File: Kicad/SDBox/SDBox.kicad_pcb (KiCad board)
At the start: 2 copper layers, 36.8 x 31.8 mm, 25 parts, among them J1 Amiga Parallel port, J2 PROG, J3 SD_Card, J4 USB_B_Micro, J5 USB_B_Mini, J6 POWER, U1 ATmega328-AU, U2 SPX3819M5-L-3-3, Y1 16M

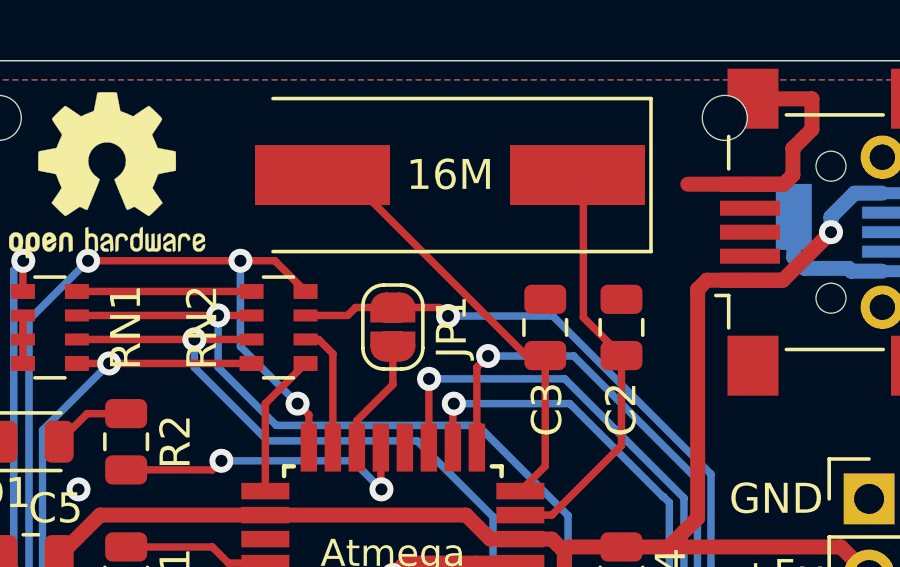
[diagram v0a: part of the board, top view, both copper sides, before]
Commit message: Added CSTCE crystal footprint
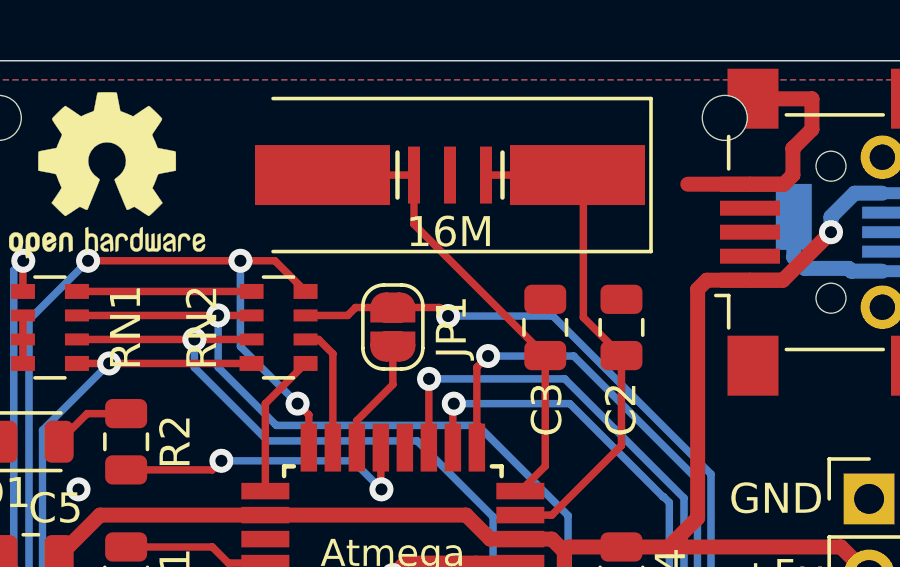
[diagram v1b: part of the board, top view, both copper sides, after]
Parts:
- added Y2: 16M, Sassa:MURATA_CSTCE, F.Cu at (126.4, 75.6)
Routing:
- net Net-(C2-Pad2): track 14.0 -> 17.0 mm
- net Net-(C3-Pad2): track 14.8 -> 15.7 mm

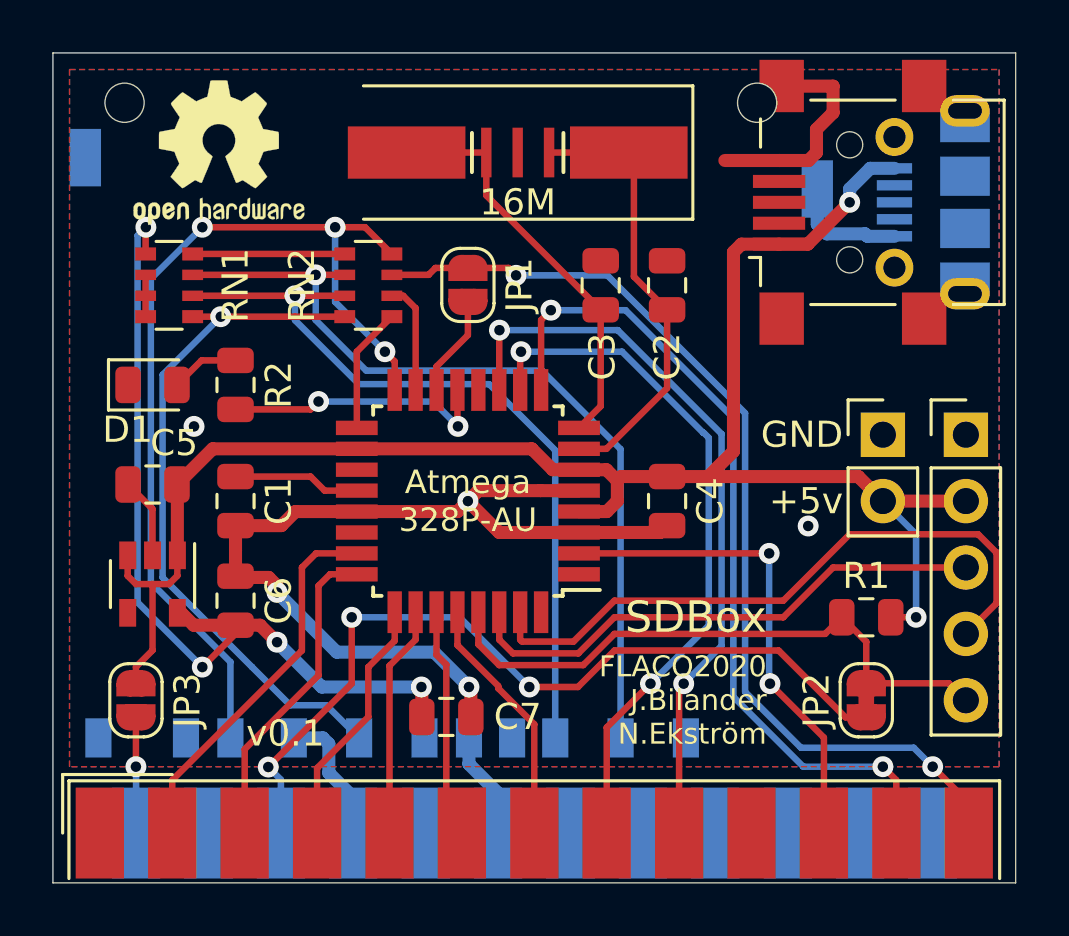
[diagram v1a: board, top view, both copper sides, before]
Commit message: Kicad : 0.2 with broken SPI programming port
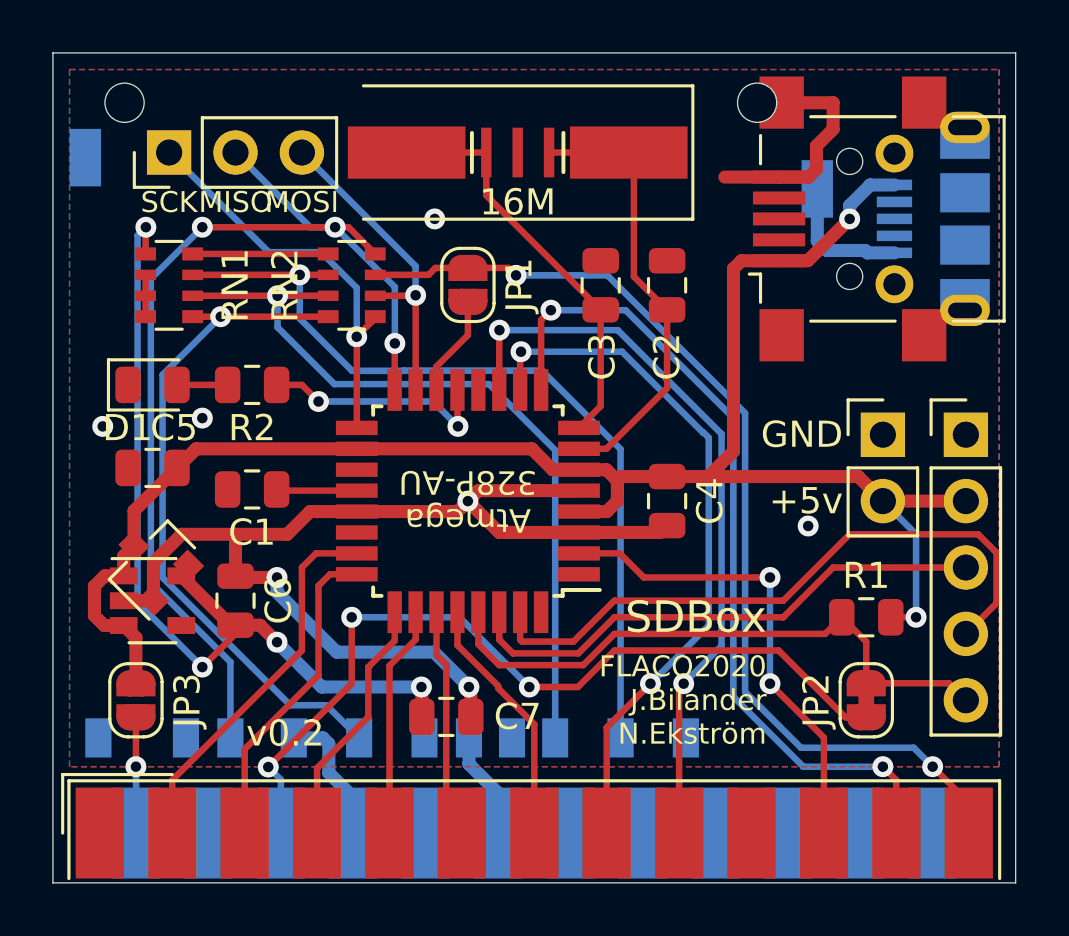
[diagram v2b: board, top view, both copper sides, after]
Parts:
- removed the J3 at (123.8, 73.7)
- added J2: SD_Card, Sassa:Conn_SDcard, B.Cu at (123.8, 73.7)
- added J7: PROG, Connector_PinHeader_2.54mm:PinHeader_1x03_P2.54mm_Vertical, F.Cu at (113.0, 75.6)
- added U20: XC6206PxxxMR, Package_TO_SOT_SMD:SOT-23, F.Cu at (112.4, 91.3)
- FID1: moved to B.Cu
- moved FID1 16.9 mm to (124.5, 89.5), turned to 180 degrees
- moved C1 0.78 mm to (116.2, 88.5), turned to 180 degrees
- moved C5 0.64 mm to (112.4, 87.6)
- moved J3 0.64 mm to (139.1, 78.1)
- moved J4 0.64 mm to (142.2, 78.1)
- moved R2 0.64 mm to (116.2, 84.5), turned to 180 degrees
- moved RN2 0.64 mm to (120.0, 80.6)
- moved U2 0.63 mm to (112.4, 92.7), turned to 0 degrees
- renumbered J5 to J3, J6 to J5, J2 to J6
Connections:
- J1 pad 1: (no net) -> Net-(J1-Pad1)
- J1 pad 10: (no net) -> Net-(J1-Pad10)
- J1 pad 15: (no net) -> Net-(J1-Pad15)
- J1 pad 23: (no net) -> Net-(J1-Pad23)
- J1 pad 24: (no net) -> Net-(J1-Pad24)
- J1 pad 25: (no net) -> Net-(J1-Pad25)
- J3 pad 2: (no net) -> Net-(J3-Pad2)
- J3 pad 3: (no net) -> Net-(J3-Pad3)
- J3 pad 4: (no net) -> Net-(J3-Pad4)
- J4 pad 2: (no net) -> Net-(J4-Pad2)
- J4 pad 3: (no net) -> Net-(J4-Pad3)
- J4 pad 4: (no net) -> Net-(J4-Pad4)
- U1 pad 1: (no net) -> Net-(U1-Pad1)
- U1 pad 12: (no net) -> Net-(U1-Pad12)
- U1 pad 19: (no net) -> Net-(U1-Pad19)
- U1 pad 22: (no net) -> Net-(U1-Pad22)
- U1 pad 32: (no net) -> Net-(U1-Pad32)
- U2 pad 4: (no net) -> Net-(U2-Pad4)
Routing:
- net /SCK: track 4.81 -> 15.7 mm, vias 0 -> 1
- net /MOSI: track 4.24 -> 12.4 mm, vias 0 -> 1
- net /MISO: track 36.5 -> 40.8 mm
- net GND: track 78.9 -> 81.9 mm, vias 5 -> 7
- net Net-(C1-Pad1): track 4.86 -> 3.09 mm
- net /LED: track 10.4 -> 8.99 mm
- net +3V3: track 34.8 -> 35.8 mm
- net Net-(D1-Pad2): track 2.63 -> 1.94 mm
- net Net-(RN1-Pad8): track 5.82 -> 5.18 mm
- net Net-(J2-Pad5): track 26.8 -> 26.1 mm
- net /SS: track 38.1 -> 38.7 mm
- net /IDLE: track 18.8 -> 18.3 mm
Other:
- board text added: "MISO"
- board text added: "MOSI"
- board text added: "SCK"
- board text added: "v0.2"
- board text removed: "v0.1"
